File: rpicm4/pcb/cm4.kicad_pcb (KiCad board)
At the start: 2 copper layers, 85.6 x 55 mm, 18 parts, among them J1 USB_C_Receptacle_USB2.0, J10 Conn_01x02_Male, J11 Conn_01x04_Male, J12 Conn_01x04_Male, J16 Conn_01x04_Male, J2 USB_C_Receptacle_USB2.0, J3 Conn_01x02_Male, J4 Conn_01x02_Male, J5 Conn_01x02_Male, J6 Conn_01x02_Male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

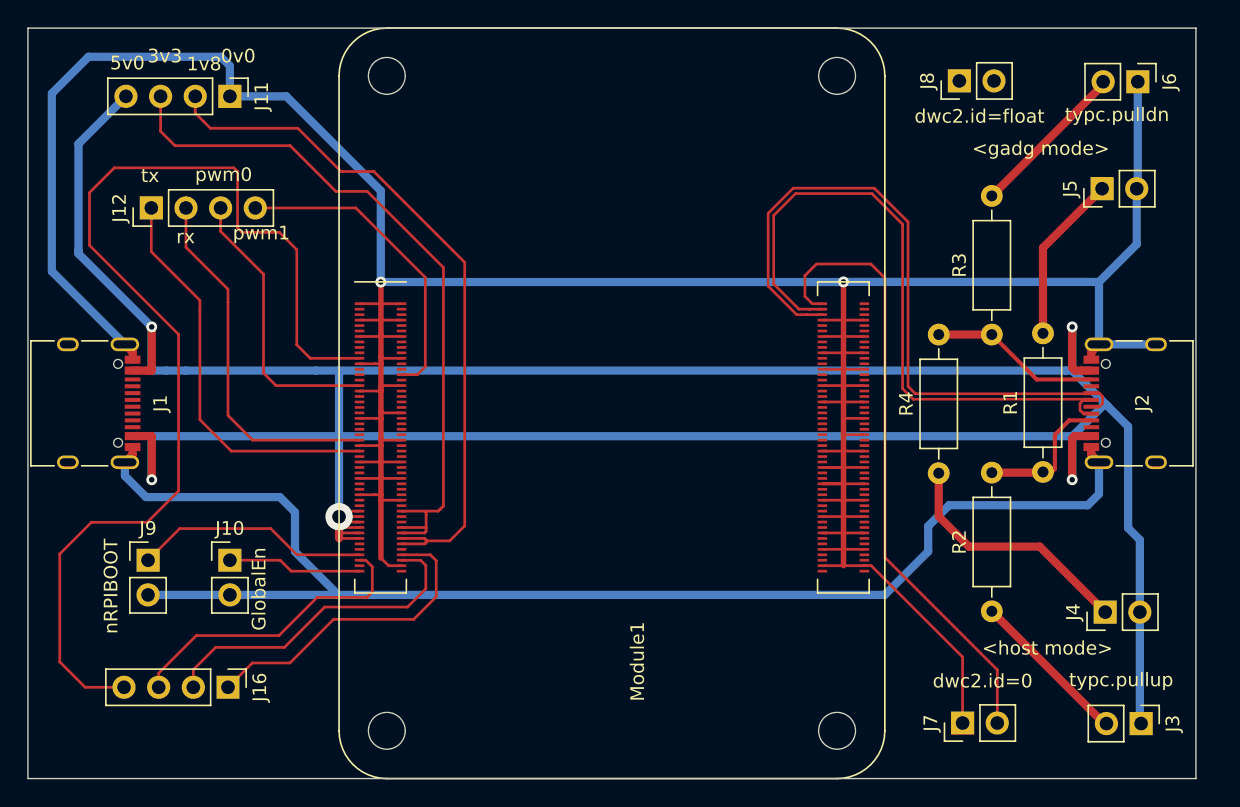
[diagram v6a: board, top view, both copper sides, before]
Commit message: rpicm4: signal@front, power@back
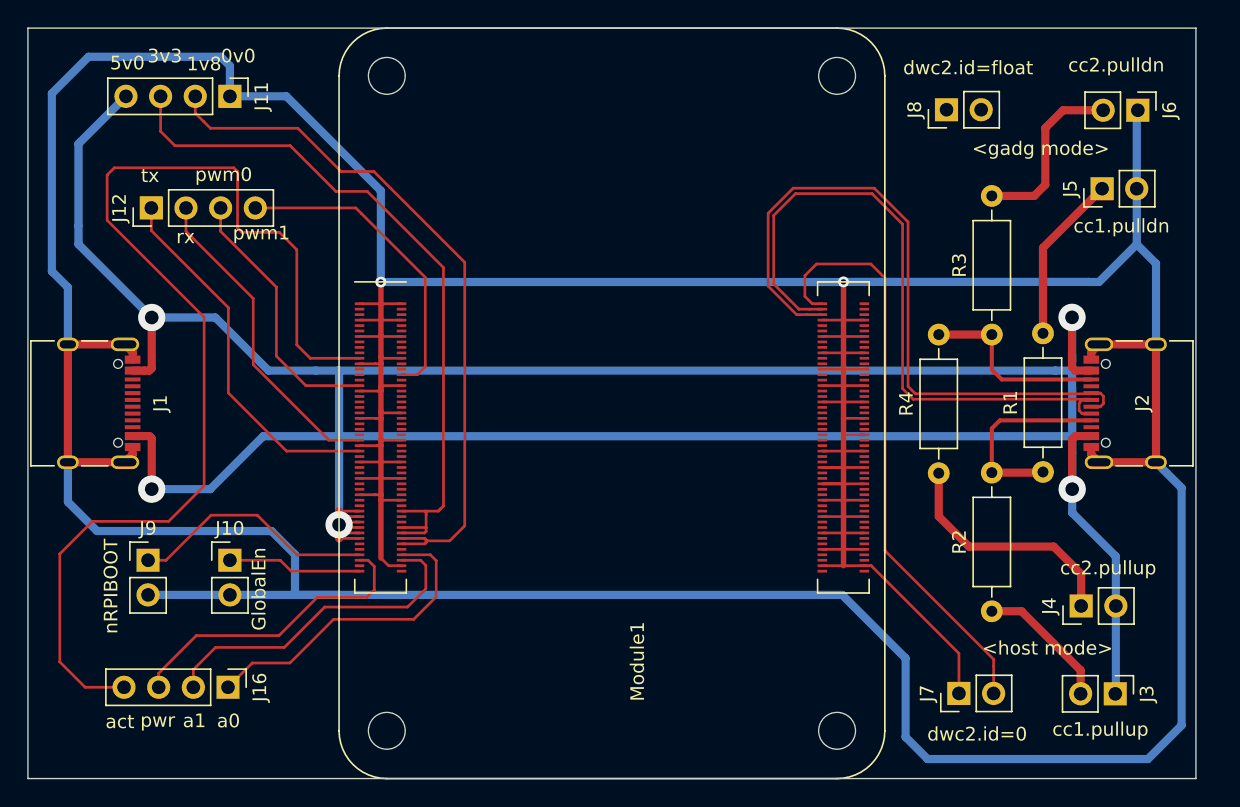
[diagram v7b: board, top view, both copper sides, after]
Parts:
- moved J3 2.89 mm to (136.9, 93.8)
- moved J8 2.31 mm to (124.5, 51.0)
- moved J7 2.19 mm to (125.4, 93.8)
- moved J6 2.09 mm to (138.5, 51.0)
- moved J4 1.82 mm to (134.4, 87.3)
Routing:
- net GND: track 377.2 -> 438.6 mm
- net +5V: track 238.5 -> 230.0 mm
- net /cc1: track 10.3 -> 15.2 mm
- net /rx: track 26.9 -> 23.6 mm
- net /tx: track 29.6 -> 27.3 mm
- net Net-(J7-Pad2): track 45.7 -> 43.4 mm
- net /cc2: track 12.5 -> 14.0 mm
- net Net-(J6-Pad2): track 11.7 -> 13.2 mm
- net /actled: track 81.4 -> 82.8 mm
- net /pwm0: track 20.8 -> 19.5 mm
- net Net-(J3-Pad2): track 11.2 -> 10.0 mm
- net /nRPIBOOT: track 17.3 -> 18.1 mm
- net Net-(J4-Pad1): track 18.3 -> 17.7 mm
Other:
- board text added: "a0"
- board text added: "a1"
- board text added: "act"
- board text added: "cc1.pulldn"
- board text added: "cc1.pullup"
- board text added: "cc2.pulldn"
- board text added: "cc2.pullup"
- board text added: "pwr"
- board text removed: "typc.pulldn"
- board text removed: "typc.pullup"

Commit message: rpicm4: fix wire
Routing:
- net GND: track 438.6 -> 427.2 mm
- net /ana0: track 23.4 -> 24.5 mm
- net /ana1: track 24.4 -> 25.5 mm
- net /tx: track 27.3 -> 26.8 mm
